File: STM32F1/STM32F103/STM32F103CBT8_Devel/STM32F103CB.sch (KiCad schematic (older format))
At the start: 25 parts, among them J1 Conn_02x03_Odd_Even, J3 Conn_02x10_Odd_Even, J6 Conn_02x05 Odd_Even, SW1 SW_Push, U1 STM32F103CBTx, Y1 8MHz, Y2 Crystal

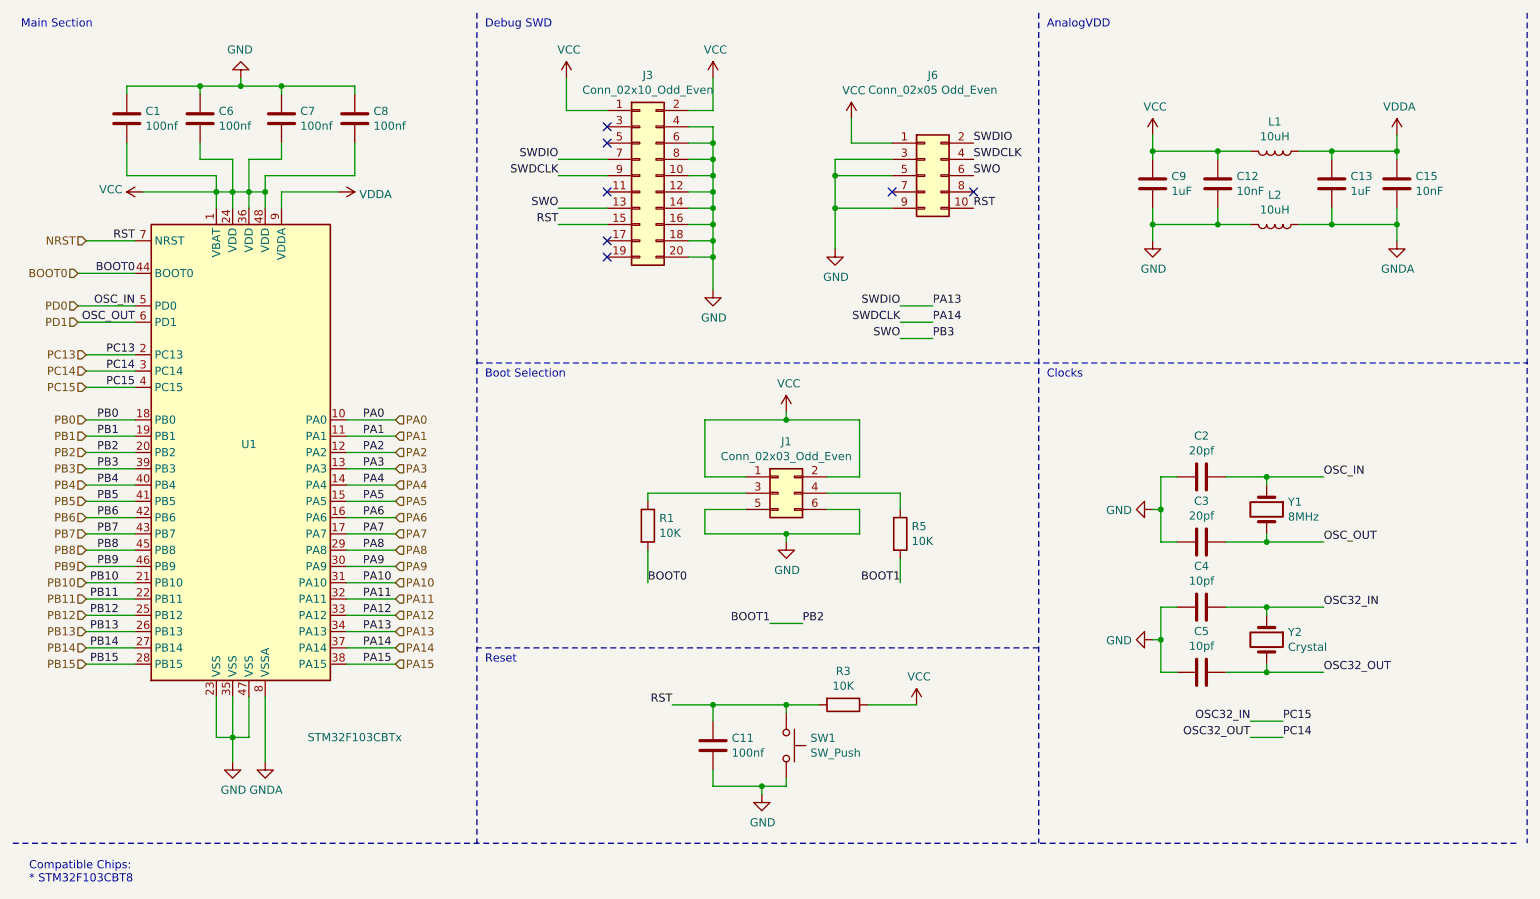
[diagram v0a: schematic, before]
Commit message: Update to dip sw and local VCC
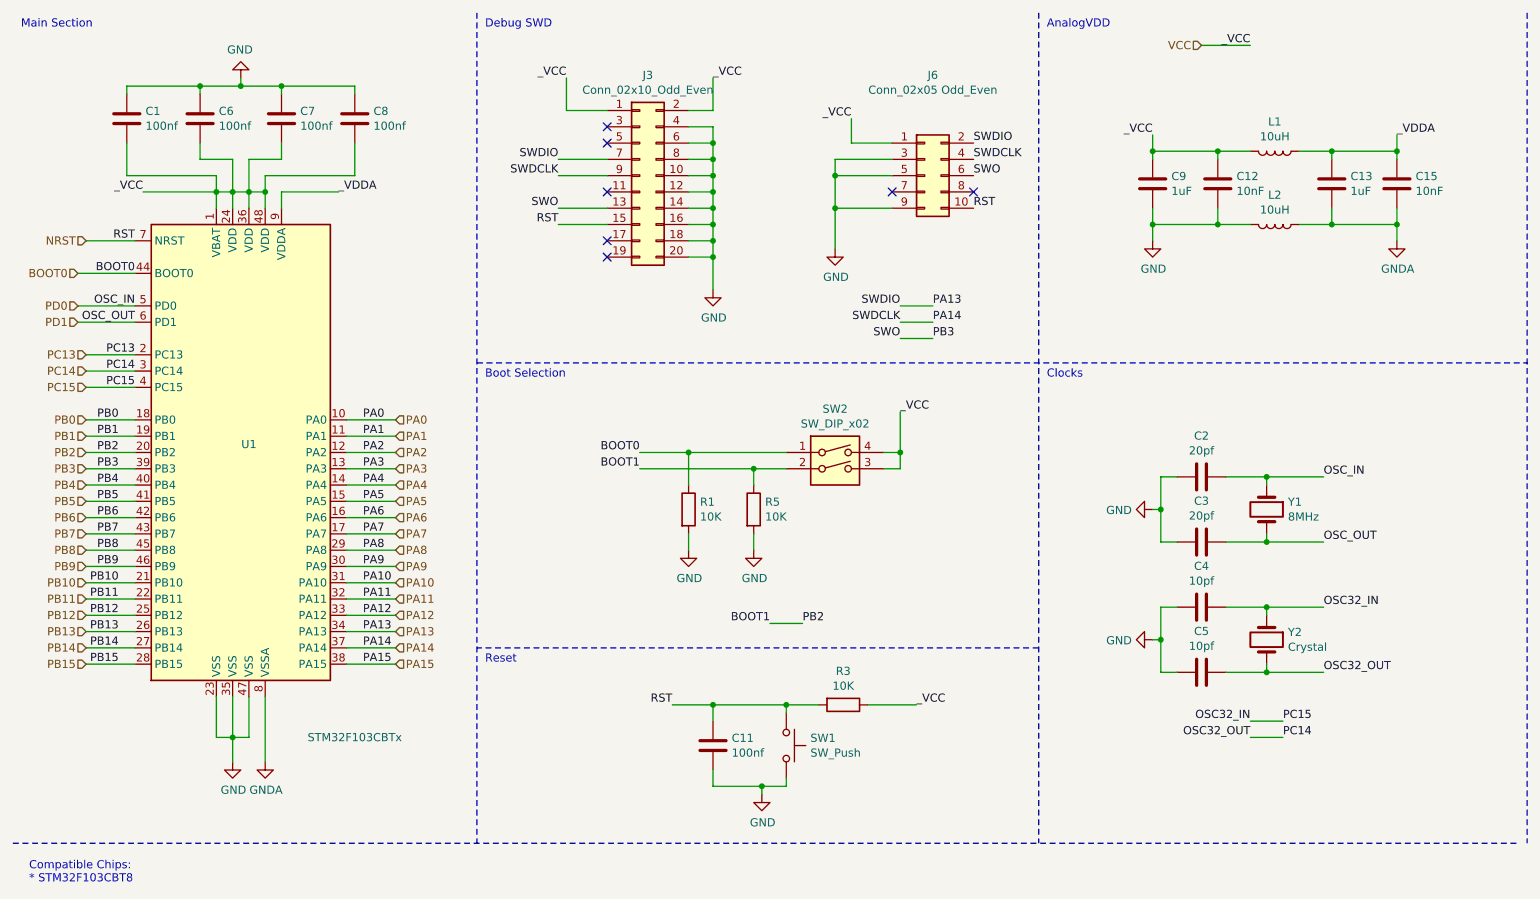
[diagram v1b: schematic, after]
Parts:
- removed J1: Conn_02x03_Odd_Even, Connector_PinHeader_2.54mm:PinHeader_2x03_P2.54mm_Vertical, symbol Connector_Generic:Conn_02x03_Odd_Even
- added SW2: SW_DIP_x02, Button_Switch_SMD:SW_DIP_SPSTx02_Slide_6.7x6.64mm_W6.73mm_P2.54mm_LowProfile_JPin, symbol Switch:SW_DIP_x02
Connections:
- net BOOT0: now also R1.1, SW2.1; no longer R1.2
- net GND: now also R1.2, R5.2
- net PB2: now also R5.1, SW2.2; no longer R5.2
- net VCC: now also SW2.3, SW2.4
- net VDDA renamed _VDDA
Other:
- moved on the sheet: R1, R5

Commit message: First version of 030
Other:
- note added: "Compatible Chips:\n* STM32F103CBT8\n* STM32F103C8T8"
- note removed: "Compatible Chips:\n* STM32F103CBT8"
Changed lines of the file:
@@
 Main Section
 Text Notes 600  5850 0    50   ~ 0
-Compatible Chips:\n* STM32F103CBT8
+Compatible Chips:\n* STM32F103CBT8\n* STM32F103C8T8
 Text Notes 3400 600  0    50   ~ 0
 Debug SWD
